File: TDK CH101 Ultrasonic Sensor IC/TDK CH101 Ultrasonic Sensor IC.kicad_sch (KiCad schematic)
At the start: 1 part, among them U1 CH101-02ABR

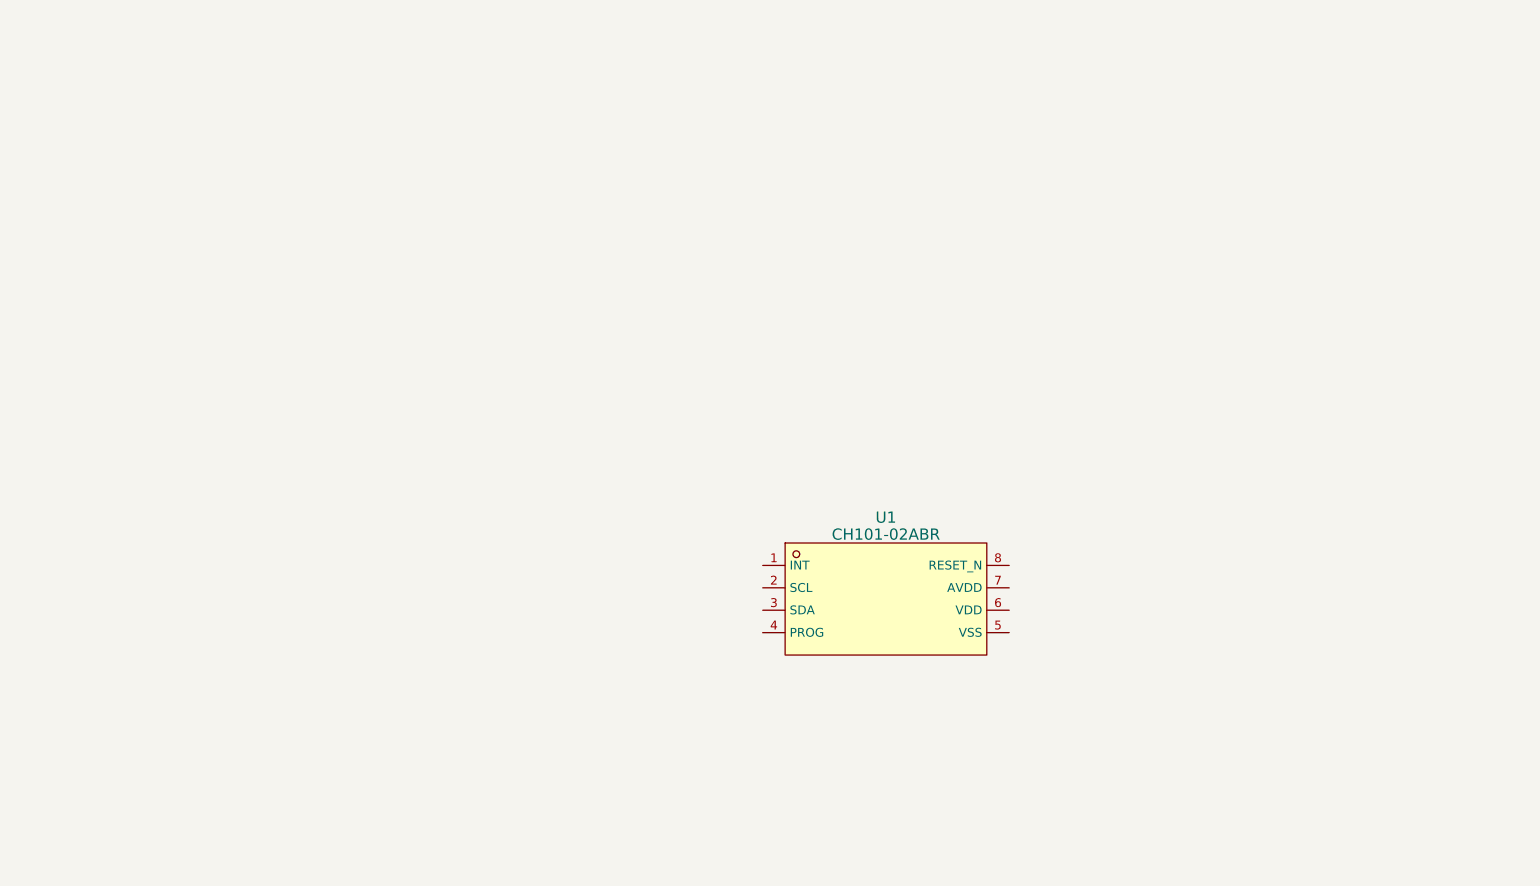
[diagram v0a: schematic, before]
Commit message: Update: TDK CH101 complete PCB
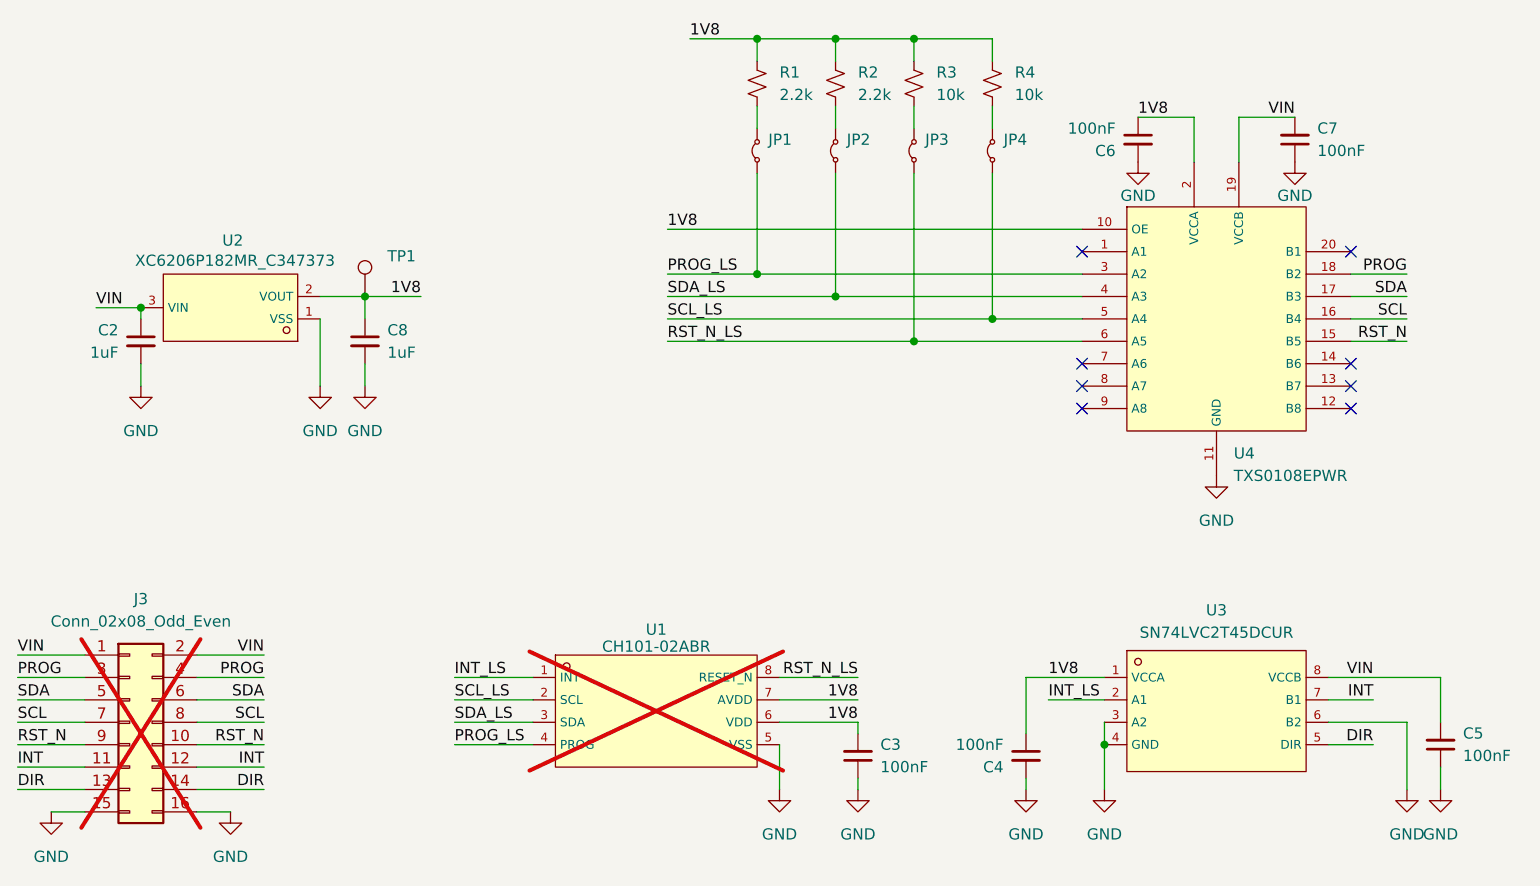
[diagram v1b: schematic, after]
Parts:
- added C2, C8: 1uF, Capacitor_SMD:C_0603_1608Metric, symbol Device:C_Small
- added C3, C4, C5, C6, C7: 100nF, Capacitor_SMD:C_0603_1608Metric, symbol Device:C_Small
- added J3: Conn_02x08_Odd_Even, Connector_PinHeader_2.54mm:PinHeader_2x08_P2.54mm_Vertical, symbol Connector_Generic:Conn_02x08_Odd_Even
- added JP1, JP2, JP3, JP4: Jumper_2_Small_Bridged, Jumper:SolderJumper-2_P1.3mm_Open_TrianglePad1.0x1.5mm, symbol Jumper:Jumper_2_Small_Bridged
- added R1, R2: 2.2k, Resistor_SMD:R_0603_1608Metric, symbol Device:R_Small_US
- added R3, R4: 10k, Resistor_SMD:R_0603_1608Metric, symbol Device:R_Small_US
- added TP1: TestPoint, TestPoint:TestPoint_Pad_1.0x1.0mm, symbol Connector:TestPoint
- added U2: XC6206P182MR_C347373, footprint:SOT-23-3_L3.0-W1.7-P0.95-LS2.9-BR, symbol Ultrasonic Sensors:XC6206P182MR_C347373
- added U3: SN74LVC2T45DCUR, footprint:VSSOP-8_L2.4-W2.1-P0.50-LS3.2-BR, symbol Ultrasonic Sensors:SN74LVC2T45DCUR
- added U4: TXS0108EPWR, footprint:TSSOP-20_L6.5-W4.4-P0.65-LS6.4-BL, symbol Ultrasonic Sensors:TXS0108EPWR
- U1: now not fitted; now left out of the parts list
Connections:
- net INT_LS: now reaches U1.1 (INT)
- net INT_LS: now also U3.2 (A1)
- net SCL_LS: now reaches U1.2 (SCL)
- net SCL_LS: now also JP4.1 (A), U4.5 (A4)
- net SDA_LS: now reaches U1.3 (SDA)
- net SDA_LS: now also JP2.1 (A), U4.4 (A3)
- net PROG_LS: now reaches U1.4 (PROG)
- net PROG_LS: now also JP1.1 (A), U4.3 (A2)
- net GND: now reaches U1.5 (VSS)
- net GND: now also C2.2, C3.1, C4.2, C5.1, C6.2, C7.1, C8.2, J3.15 (Pin_15), J3.16 (Pin_16), U2.1 (VSS), U3.3 (A2), U3.4 (GND), U3.6 (B2), U4.11 (GND)
- net 1V8: now reaches U1.6 (VDD)
- net 1V8: now also U1.7 (AVDD), C3.2, C4.1, C6.1, C8.1, R1.1, R2.1, R3.1, R4.1, TP1.1, U2.2 (VOUT), U3.1 (VCCA), U4.10 (OE), U4.2 (VCCA)
- net RST_N_LS: now reaches U1.8 (RESET_N)
- net RST_N_LS: now also JP3.1 (A), U4.6 (A5)
- new net: JP3.2 (B), R3.2
- new net: JP1.2 (B), R1.2
- new net: JP2.2 (B), R2.2
- new net: JP4.2 (B), R4.2
- new net DIR: J3.13 (Pin_13), J3.14 (Pin_14), U3.5 (DIR)
- new net INT: J3.11 (Pin_11), J3.12 (Pin_12), U3.7 (B1)
- new net PROG: J3.3 (Pin_3), J3.4 (Pin_4), U4.18 (B2)
- new net RST_N: J3.10 (Pin_10), J3.9 (Pin_9), U4.15 (B5)
- new net SCL: J3.7 (Pin_7), J3.8 (Pin_8), U4.16 (B4)
- new net SDA: J3.5 (Pin_5), J3.6 (Pin_6), U4.17 (B3)
- new net VIN: C2.1, C5.2, C7.2, J3.1 (Pin_1), J3.2 (Pin_2), U2.3 (VIN), U3.8 (VCCB), U4.19 (VCCB)
- no-connect marks 0 -> 8

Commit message: Update: CH101 production settings
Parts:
- JP1, JP2, JP3, JP4: now not fitted; now left out of the parts list
- TP1: now not fitted
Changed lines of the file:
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@@
 		(at 68.58 67.31 0)
 		(unit 1)
-		(exclude_from_sim no)
-		(in_bom yes)
-		(on_board yes)
-		(dnp no)
+		(exclude_from_sim yes)
+		(in_bom yes)
+		(on_board yes)
+		(dnp yes)
 		(property "Reference" "TP1"
 			(at 71.12 62.7379 0)
@@
 		(unit 1)
 		(exclude_from_sim no)
-		(in_bom yes)
-		(on_board yes)
-		(dnp no)
+		(in_bom no)
+		(on_board yes)
+		(dnp yes)
 		(fields_autoplaced yes)
 		(property "Reference" "JP1"
@@
 		(unit 1)
 		(exclude_from_sim no)
-		(in_bom yes)
-		(on_board yes)
-		(dnp no)
+		(in_bom no)
+		(on_board yes)
+		(dnp yes)
 		(fields_autoplaced yes)
 		(property "Reference" "JP3"
@@
 		(unit 1)
 		(exclude_from_sim no)
-		(in_bom yes)
-		(on_board yes)
-		(dnp no)
+		(in_bom no)
+		(on_board yes)
+		(dnp yes)
 		(fields_autoplaced yes)
 		(property "Reference" "JP2"
@@
 		(unit 1)
 		(exclude_from_sim no)
-		(in_bom yes)
-		(on_board yes)
-		(dnp no)
+		(in_bom no)
+		(on_board yes)
+		(dnp yes)
 		(fields_autoplaced yes)
 		(property "Reference" "JP4"
